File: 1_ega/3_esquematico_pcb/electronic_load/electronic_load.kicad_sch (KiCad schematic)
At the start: 31 parts, among them J1 Encoder, J2 LCD_I2C, J3 GND, J4 MOS_GATE, J5 Isense, J6 Vload_LPF, J7 5V, J8 MOS_LPF, Q1 IRF540N, SW1 BTN_MENU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

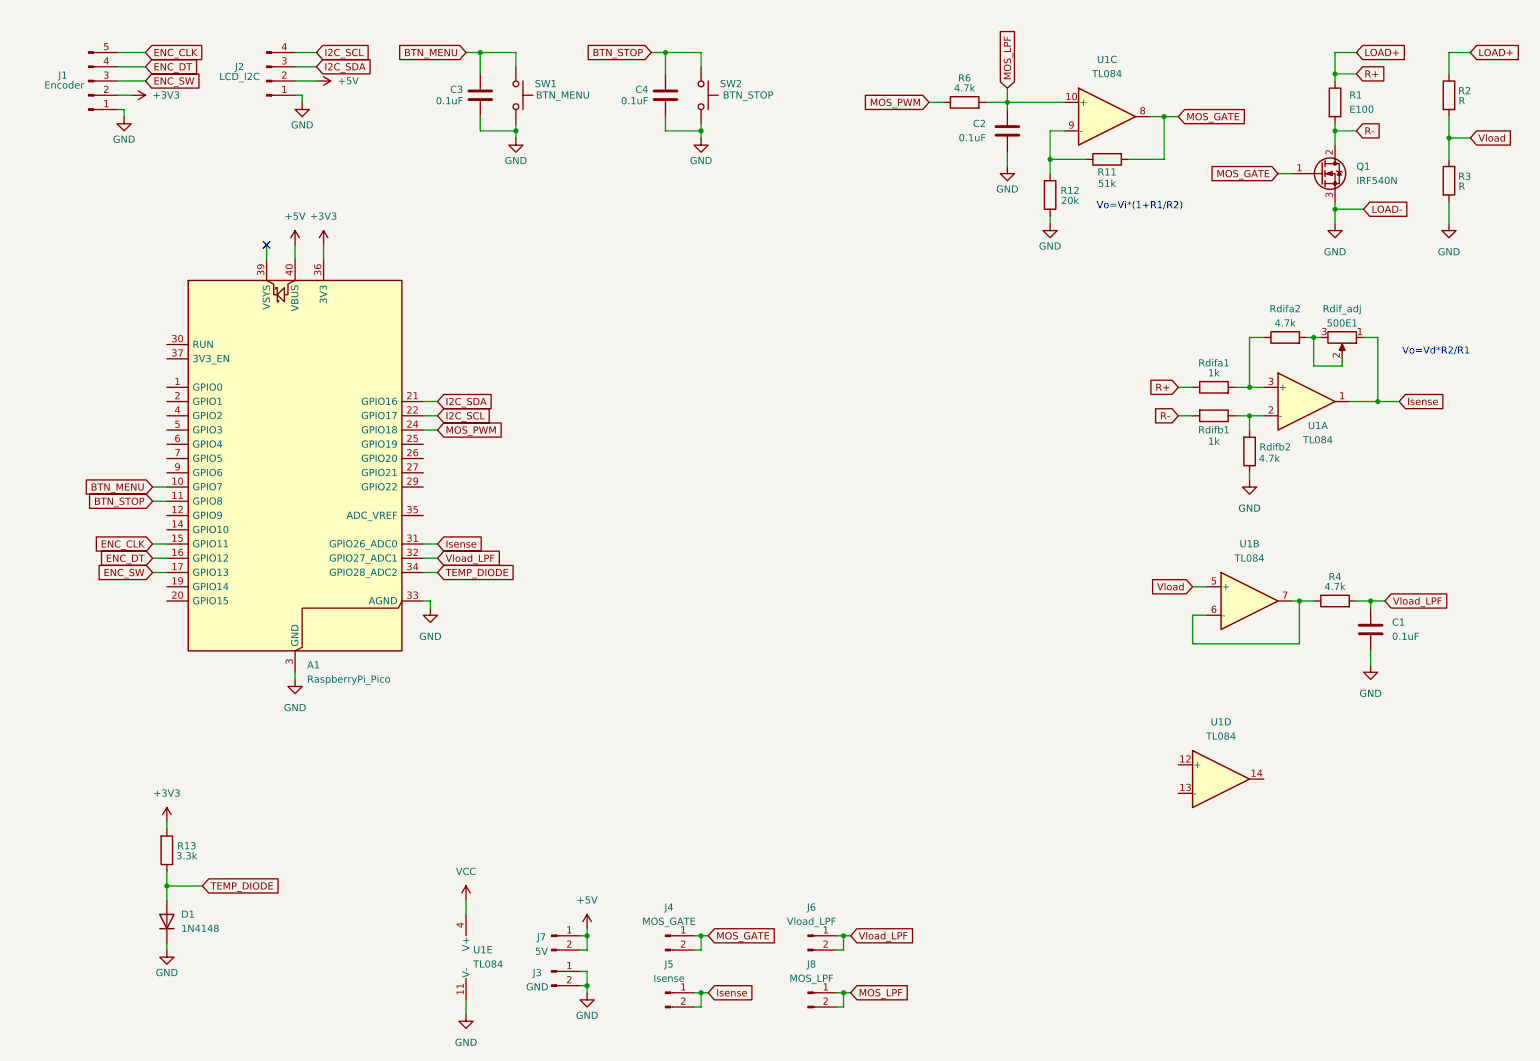
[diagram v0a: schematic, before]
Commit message: feat: primera version del esquematico con valores calculados
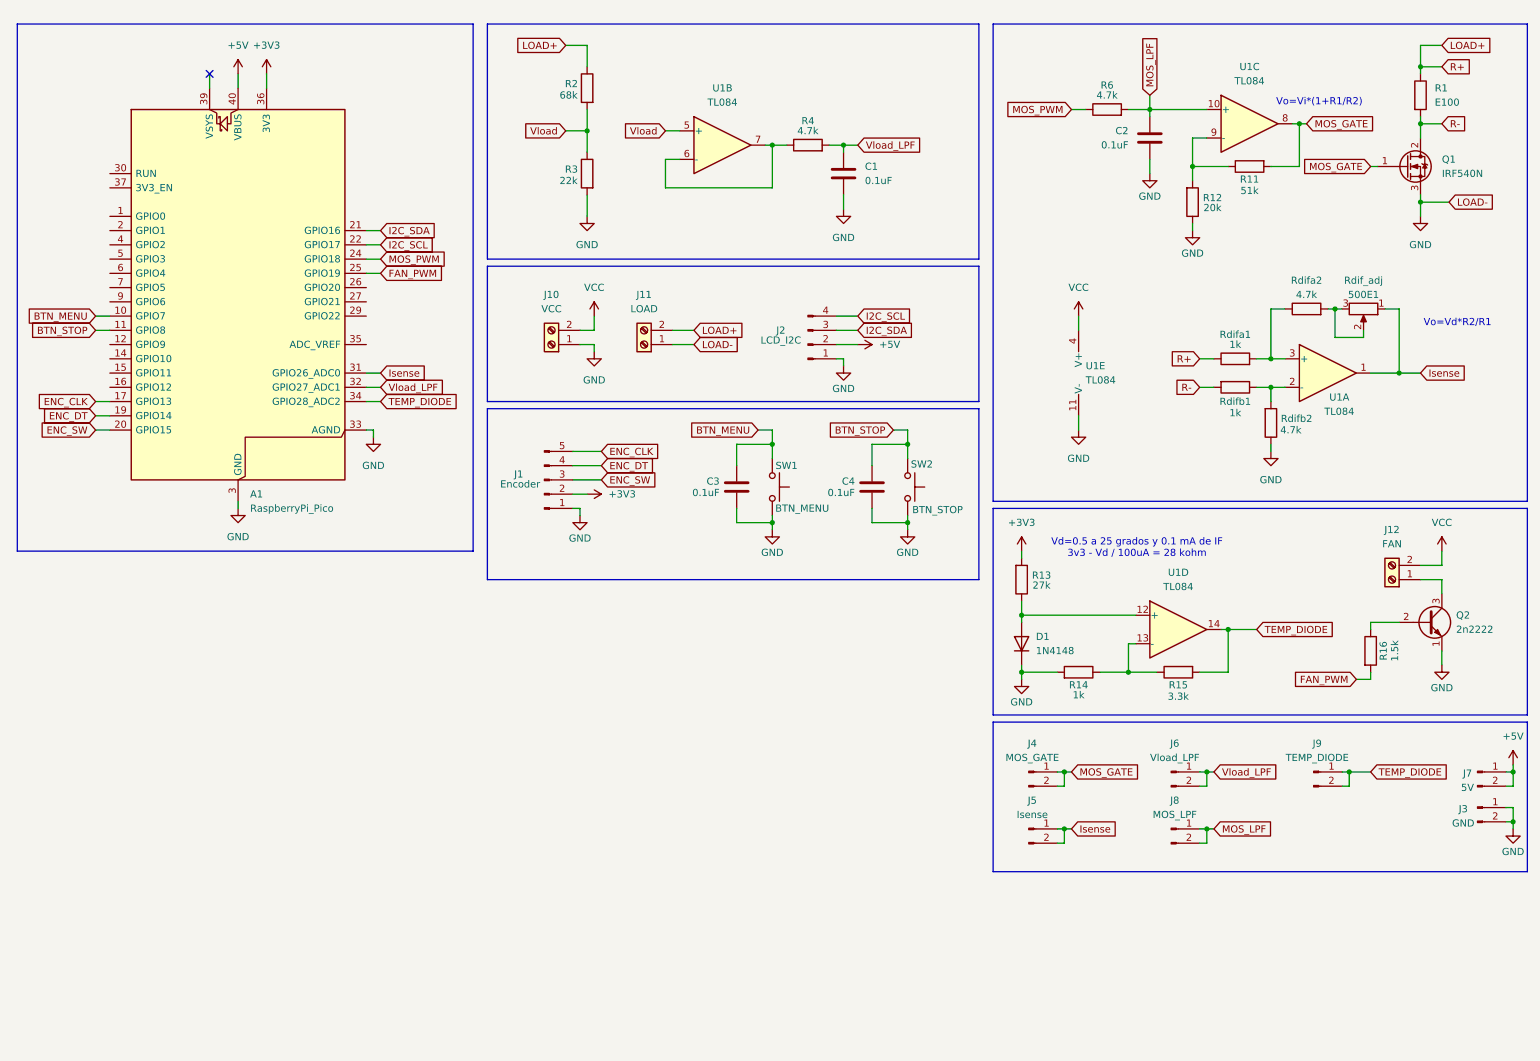
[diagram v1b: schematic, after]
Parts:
- added J10: VCC, TerminalBlock_Phoenix:TerminalBlock_Phoenix_MKDS-1,5-2-5.08_1x02_P5.08mm_Horizontal, symbol Connector:Screw_Terminal_01x02
- added J11: LOAD, TerminalBlock_Phoenix:TerminalBlock_Phoenix_MKDS-1,5-2-5.08_1x02_P5.08mm_Horizontal, symbol Connector:Screw_Terminal_01x02
- added J12: FAN, TerminalBlock_Phoenix:TerminalBlock_Phoenix_MKDS-1,5-2-5.08_1x02_P5.08mm_Horizontal, symbol Connector:Screw_Terminal_01x02
- added J9: TEMP_DIODE, Connector_PinSocket_2.54mm:PinSocket_1x02_P2.54mm_Vertical, symbol Connector:Conn_01x02_Pin
- added Q2: 2n2222, Package_TO_SOT_THT:TO-92L_Inline_Wide, symbol Transistor_BJT:2N2219
- added R14: 1k, Resistor_THT:R_Axial_DIN0207_L6.3mm_D2.5mm_P10.16mm_Horizontal, symbol Device:R
- added R15: 3.3k, Resistor_THT:R_Axial_DIN0207_L6.3mm_D2.5mm_P10.16mm_Horizontal, symbol Device:R
- added R16: 1.5k, Resistor_THT:R_Axial_DIN0207_L6.3mm_D2.5mm_P10.16mm_Horizontal, symbol Device:R
- R13: value 3.3k -> 27k
- R2: value R -> 68k
- R3: value R -> 22k
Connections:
- net ENC_CLK: now also A1.17 (GPIO13); no longer A1.15 (GPIO11)
- net ENC_DT: now also A1.19 (GPIO14); no longer A1.16 (GPIO12)
- net ENC_SW: now also A1.20 (GPIO15); no longer A1.17 (GPIO13)
- net GND: now also J10.1 (Pin_1), J11.1 (Pin_1), Q2.1 (E), R14.2
- net LOAD+: now also J11.2 (Pin_2)
- net TEMP_DIODE: now also U1.14, J9.1 (Pin_1), J9.2 (Pin_2), R15.2; no longer D1.2 (A), R13.1
- net VCC: now also J10.2 (Pin_2), J12.2 (Pin_2)
- net at U1.12 (+): now also D1.2 (A), R13.1
- net at U1.13 (-): now also R14.1, R15.1
- net FAN_PWM: now reaches A1.25 (GPIO19)
- net FAN_PWM: now also R16.2
- new net: Q2.2 (B), R16.1
- new net: J12.1 (Pin_1), Q2.3 (C)
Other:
- note added: "Vd=0.5 a 25 grados y 0.1 mA de IF 3v3 - Vd / 100uA = 28 kohm"
- moved on the sheet: 500E1, A1, C1, C2, C3, C4, D1, J1, J2, J3, J4, J5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

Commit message: add: diagrama de conexiones y modificar firmware
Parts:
- added J13: RTC_I2C, Connector_PinSocket_2.54mm:PinSocket_1x04_P2.54mm_Vertical, symbol Connector:Conn_01x04_Pin
- added R17: 10k, Resistor_THT:R_Axial_DIN0207_L6.3mm_D2.5mm_P10.16mm_Horizontal, symbol Device:R
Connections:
- net +3V3: now also J13.2 (Pin_2)
- net GND: now also J13.1 (Pin_1)
- net I2C_SCL: now also J13.4 (Pin_4)
- net I2C_SDA: now also J13.3 (Pin_3)
- net MOS_GATE: now also R17.2
- net R-: now also R17.1
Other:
- note added: "Vo=Vi*(1+R1/R2) Av=3.55 Vomax = 11.7"
- note removed: "Vo=Vi*(1+R1/R2)"
- moved on the sheet: C2, J10, J11, J2, R11, R12, R6, U1C

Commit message: mod: change TL084 for LM324
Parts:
- removed U1: TL084, Package_DIP:DIP-14_W7.62mm_LongPads, symbol Amplifier_Operational:TL084
- added U1: LM324, Package_DIP:DIP-14_W7.62mm_Socket_LongPads, symbol Amplifier_Operational:LM324
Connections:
- net GND: now also U1.11 (V-)
- net Isense: now also U1.7
- net MOS_GATE: now also U1.1
- net MOS_LPF: now also U1.3 (+)
- net TEMP_DIODE: now also U1.8
- net VCC: now also U1.4 (V+)
- net Vload: now also U1.12 (+)
- net at Rdifb1.1, Rdifb2.2: now also U1.6 (-)
- net at D1.2 (A), R13.1: now also U1.10 (+)
- net at R14.1, R15.1: now also U1.9 (-)
- net at R11.1, R12.2: now also U1.2 (-)
- net at Rdifa1.2, Rdifa2.1: now also U1.5 (+)
- net at R4.1: now also U1.13 (-), U1.14

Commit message: pruebas esquematico
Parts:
- removed 500E1: Rdif_adj, Connector_Molex:Molex_KK-254_AE-6410-03A_1x03_P2.54mm_Vertical, symbol Device:R_Potentiometer
- removed D1: 1N4148, Diode_THT:D_DO-35_SOD27_P7.62mm_Horizontal, symbol Diode:1N4148
- removed R13: 27k, Resistor_THT:R_Axial_DIN0207_L6.3mm_D2.5mm_P10.16mm_Horizontal, symbol Device:R
- removed Rdifa1, Rdifb1: 1k, Resistor_THT:R_Axial_DIN0207_L6.3mm_D2.5mm_P10.16mm_Horizontal, symbol Device:R
- removed Rdifa2, Rdifb2: 4.7k, Resistor_THT:R_Axial_DIN0207_L6.3mm_D2.5mm_P10.16mm_Horizontal, symbol Device:R
- removed U1: LM324, Package_DIP:DIP-14_W7.62mm_Socket_LongPads, symbol Amplifier_Operational:LM324
- added D2: 1N4148, Diode_THT:D_DO-35_SOD27_P7.62mm_Horizontal, symbol Diode:1N4148
- added Q3, Q4: BC327, Package_TO_SOT_THT:TO-92_Inline, symbol Transistor_BJT:BC327
- added R19: 22k, Resistor_THT:R_Axial_DIN0207_L6.3mm_D2.5mm_P10.16mm_Horizontal, symbol Device:R
- added R20, R21: 4.7k, Resistor_THT:R_Axial_DIN0207_L6.3mm_D2.5mm_P10.16mm_Horizontal, symbol Device:R
- added R25, R27: 33k, Resistor_THT:R_Axial_DIN0207_L6.3mm_D2.5mm_P10.16mm_Horizontal, symbol Device:R
- added R26, R28: 3k3, Resistor_THT:R_Axial_DIN0207_L6.3mm_D2.5mm_P10.16mm_Horizontal, symbol Device:R
- added Rinst_a1: 820, Resistor_THT:R_Axial_DIN0207_L6.3mm_D2.5mm_P10.16mm_Horizontal, symbol Device:R
- added Rinst_b1, Rinst_b2: 5k1, Resistor_THT:R_Axial_DIN0207_L6.3mm_D2.5mm_P10.16mm_Horizontal, symbol Device:R
- added U1: LM358, symbol Amplifier_Operational:LM358
- added U2: LM324, symbol Amplifier_Operational:LM324
- added U3: LM35-LP, Package_TO_SOT_THT:TO-92_Inline, symbol Sensor_Temperature:LM35-LP
- R14: value 1k -> 5k1
- R15: value 3.3k -> 1k
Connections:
- net +3V3: now also R20.1, R21.1
- net +5V: now also A1.39 (VSYS), U2.4 (V+), U3.1 (+V_{S}); no longer A1.40 (VBUS)
- net GND: now also R1.2, D2.1 (K), R19.2, R28.1, U1.4 (V-), U2.11 (V-), U2.5 (+), U3.3 (GND); no longer A1.33 (AGND), Q1.3 (S)
- net Isense: now also R26.2, U2.8
- net LOAD+: now also Q1.2 (D), R17.1; no longer R1.1
- net MOS_GATE: now also U1.1
- net MOS_LPF: now also U1.3 (+)
- net TEMP_DIODE: now also U2.14, U3.2 (V_{OUT})
- net VCC: now also U1.8 (V+)
- net Vload: now also U1.5 (+)
- net at R11.1, R12.2: now also U1.2 (-)
- net at R14.1, R15.1: now also U2.13 (-)
- net at R4.1: now also U1.6 (-), U1.7
- removed net R-: Q1.2 (D), R1.2, R17.1
- new net: Rinst_a1.1, Rinst_b2.1, U2.6 (-)
- new net: Rinst_a1.2, Rinst_b1.1, U2.2 (-)
- new net: R27.1, Rinst_b1.2, U2.1
- new net: R27.2, R28.2, U2.10 (+)
- new net: R25.2, R26.1, U2.9 (-)
- new net: Q3.2 (B), Q4.1 (C), Q4.2 (B), R19.1
- new net: R25.1, Rinst_b2.2, U2.7
- new net: Q3.3 (E), R20.2
- new net: Q4.3 (E), R21.2
- new net R+: Q1.3 (S), R1.1, U2.3 (+)
- new net V_DIODE: D2.2 (A), Q3.1 (C), U2.12 (+)
- no-connect marks 1 -> 19
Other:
- note added: "Vo=Vd*(1+2Rb/Ra)*R2/R1 Vdmax=25mV Av=132"
- note removed: "Vo=Vd*R2/R1"
- moved on the sheet: C2, Q1, R1, R11, R12, R14, R15, R17, R6

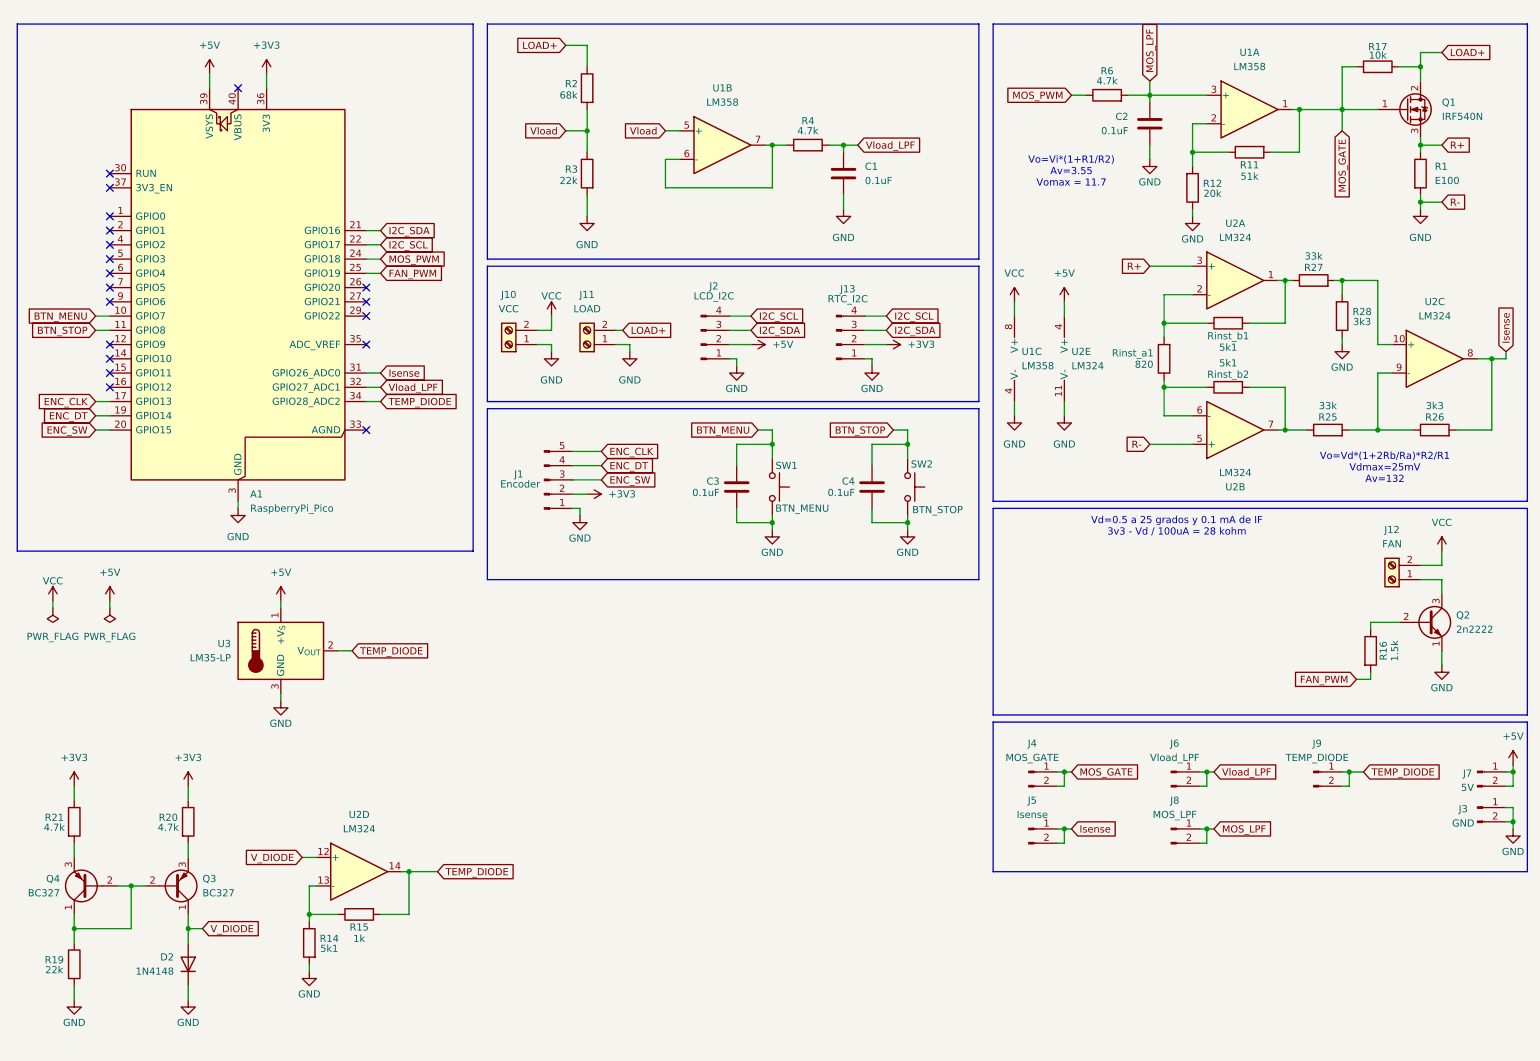
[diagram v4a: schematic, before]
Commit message: rev: modify the values and validate current source for 1N4148
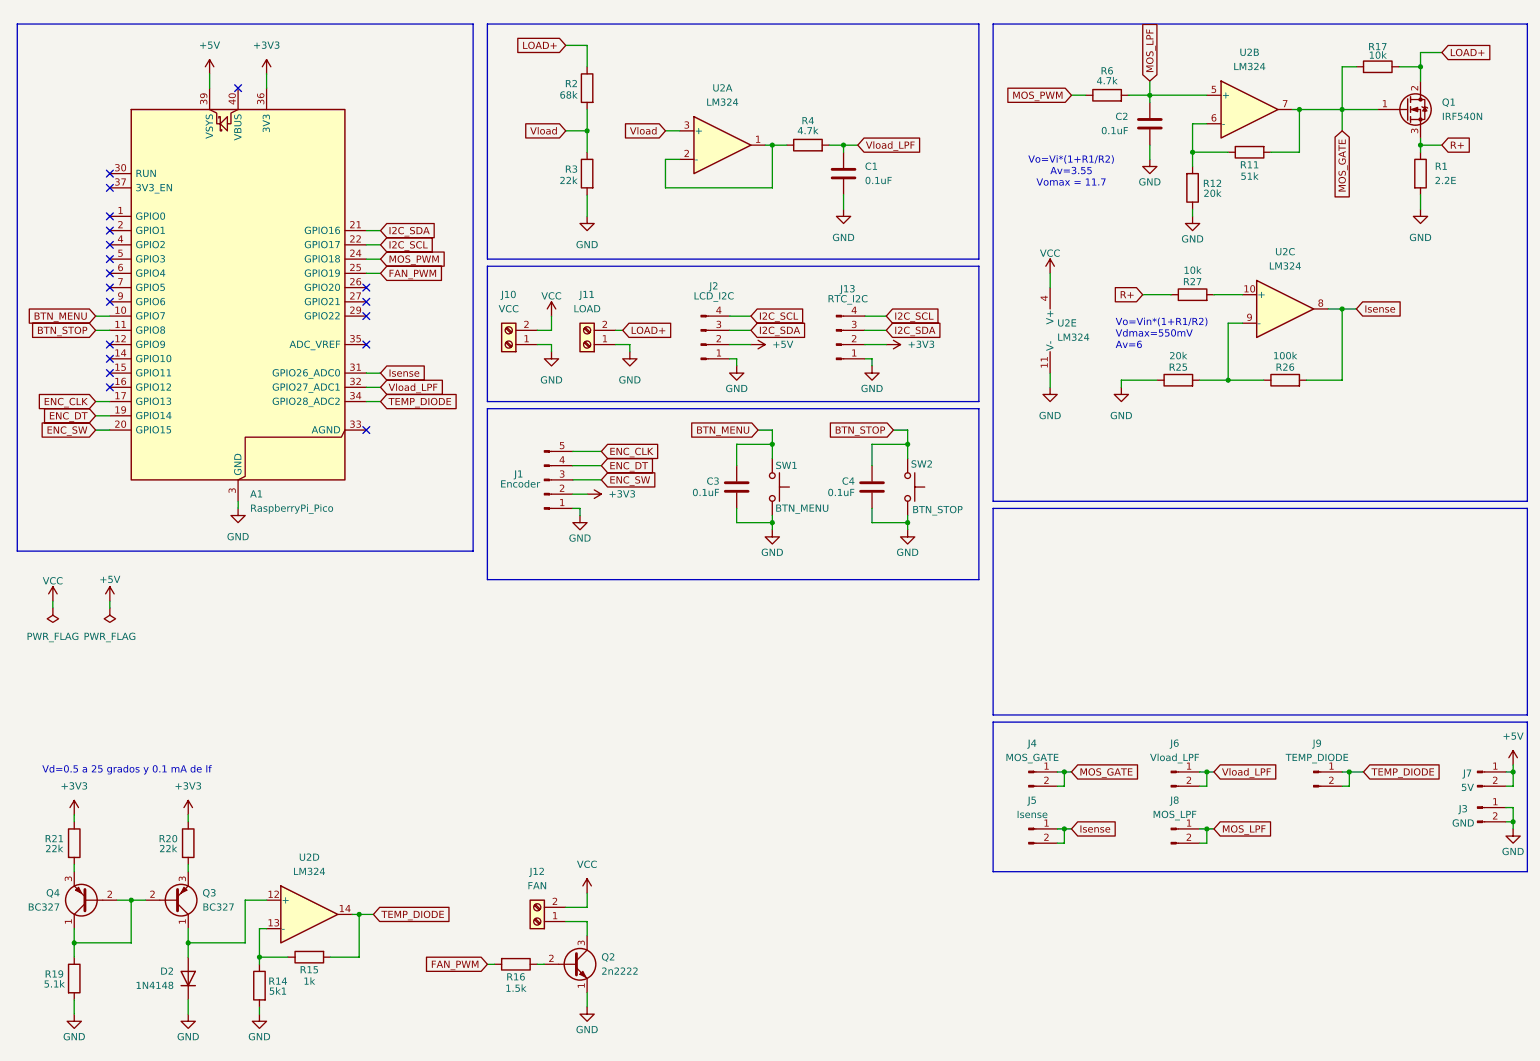
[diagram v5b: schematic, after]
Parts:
- removed R28: 3k3, Resistor_THT:R_Axial_DIN0207_L6.3mm_D2.5mm_P10.16mm_Horizontal, symbol Device:R
- removed Rinst_a1: 820, Resistor_THT:R_Axial_DIN0207_L6.3mm_D2.5mm_P10.16mm_Horizontal, symbol Device:R
- removed Rinst_b1, Rinst_b2: 5k1, Resistor_THT:R_Axial_DIN0207_L6.3mm_D2.5mm_P10.16mm_Horizontal, symbol Device:R
- removed U1: LM358, symbol Amplifier_Operational:LM358
- removed U3: LM35-LP, Package_TO_SOT_THT:TO-92_Inline, symbol Sensor_Temperature:LM35-LP
- R1: value E100 -> 2.2E
- R19: value 22k -> 5.1k
- R20, R21: value 4.7k -> 22k
- R25: value 33k -> 20k
- R26: value 3k3 -> 100k
- R27: value 33k -> 10k
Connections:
- net +5V: no longer U2.4 (V+)
- net GND: now also R25.1; no longer U2.5 (+)
- net MOS_GATE: now also U2.7
- net MOS_LPF: now also U2.5 (+)
- net R+: now also R27.1; no longer U2.3 (+)
- net VCC: now also U2.4 (V+)
- net Vload: now also U2.3 (+)
- net at U2.6 (-): now also R11.1, R12.2
- net at U2.2 (-): now also R4.1, U2.1
- net V_DIODE: no longer names the net of D2.2 (A), Q3.1 (C), U2.12 (+)
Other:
- note added: "Vd=0.5 a 25 grados y 0.1 mA de If"
- note added: "Vo=Vin*(1+R1/R2) Vdmax=550mV Av=6"
- note removed: "Vd=0.5 a 25 grados y 0.1 mA de IF 3v3 - Vd / 100uA = 28 kohm"
- note removed: "Vo=Vd*(1+2Rb/Ra)*R2/R1 Vdmax=25mV Av=132"
- moved on the sheet: D2, J12, Q2, Q3, Q4, R14, R15, R16, R19, R20, R21, R25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
